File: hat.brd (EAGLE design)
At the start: 65 x 56.5 mm, 40 parts, among them U1 ADS1115IDGST, U2 MCP2515-I/SO, U3 MCP2551, X1 16Mhz

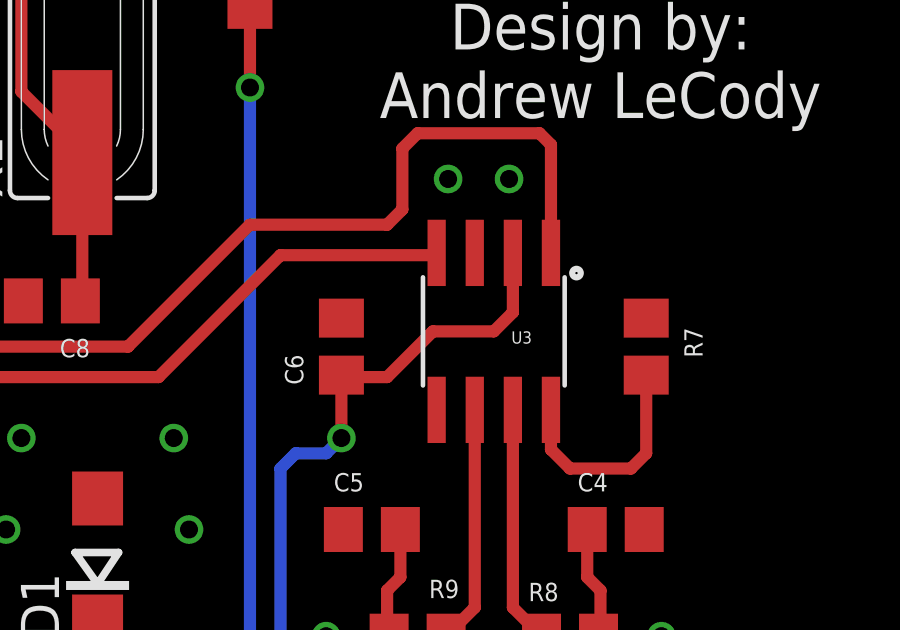
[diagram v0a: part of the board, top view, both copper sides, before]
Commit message: Fixed power for MCP2551
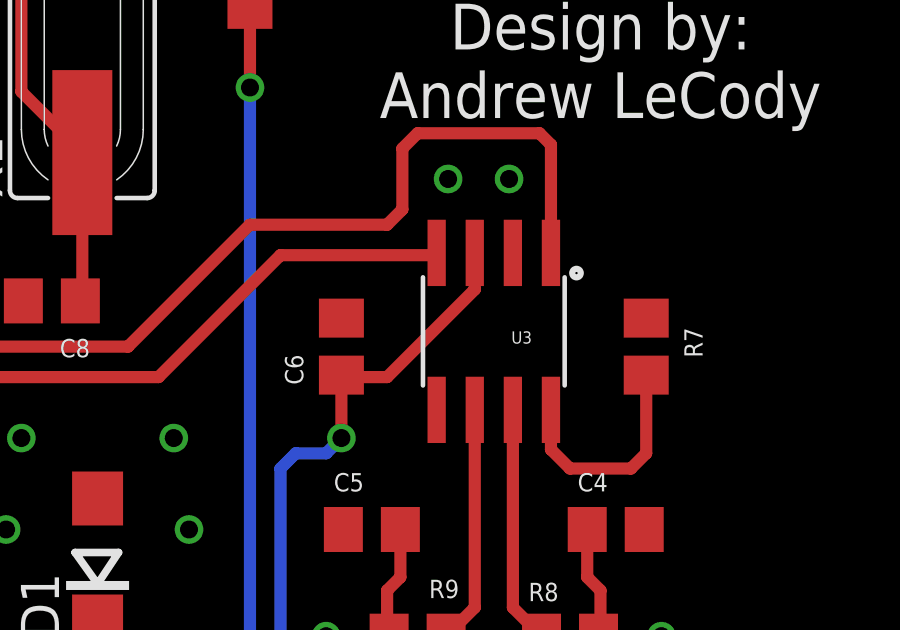
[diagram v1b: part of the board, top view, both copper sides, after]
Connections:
- net 5V: now also U3.3; no longer U3.2
- net GND: now also U3.2; no longer U3.3
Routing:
- net 5V: track 127.7 -> 126.0 mm
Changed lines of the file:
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@@
 <?xml version="1.0" encoding="utf-8"?>
 <!DOCTYPE eagle SYSTEM "eagle.dtd">
-<eagle version="8.0.1">
+<eagle version="7.7.0">
 <drawing>
 <settings>
@@
 <contactref element="D1" pad="A"/>
 <contactref element="R7" pad="1"/>
-<contactref element="U3" pad="3"/>
 <contactref element="R11" pad="1"/>
 <contactref element="U2" pad="9"/>
@@
 <contactref element="D3" pad="3"/>
 <contactref element="I2C" pad="1"/>
+<contactref element="U3" pad="2"/>
 </signal>
 <signal name="TXD">
@@
 <contactref element="RPI1" pad="4"/>
 <contactref element="RPI1" pad="2"/>
-<contactref element="U3" pad="2"/>
 <wire x1="8.37" y1="53.77" x2="8.37" y2="53.582" width="0.4064" layer="16"/>
 <wire x1="8.37" y1="53.582" x2="7.112" y2="52.324" width="0.4064" layer="16"/>
@@
 <wire x1="45.72" y1="19.878" x2="45.786" y2="19.812" width="0.4064" layer="1"/>
 <wire x1="45.786" y1="19.812" x2="47.244" y2="19.812" width="0.4064" layer="1"/>
-<wire x1="47.244" y1="19.812" x2="48.768" y2="21.336" width="0.4064" layer="1"/>
-<wire x1="48.768" y1="21.336" x2="50.8" y2="21.336" width="0.4064" layer="1"/>
-<wire x1="50.8" y1="21.336" x2="51.435" y2="21.971" width="0.4064" layer="1"/>
-<wire x1="51.435" y1="21.971" x2="51.435" y2="23.9522" width="0.4064" layer="1"/>
+<wire x1="47.244" y1="19.812" x2="50.165" y2="22.733" width="0.4064" layer="1"/>
+<contactref element="U3" pad="3"/>
+<wire x1="50.165" y1="22.733" x2="50.165" y2="23.9522" width="0.4064" layer="1"/>
 </signal>
 <signal name="TXCAN">
